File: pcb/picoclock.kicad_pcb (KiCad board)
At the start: 2 copper layers, 175.8 x 64 mm, 63 parts, among them J1 UART, J10 USB, J11 Alt Power, J12 PWM, J2 AUDIO, J3 xx, J4 xx, J5 Power In, J6 USB_C_Receptacle, J7 xx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

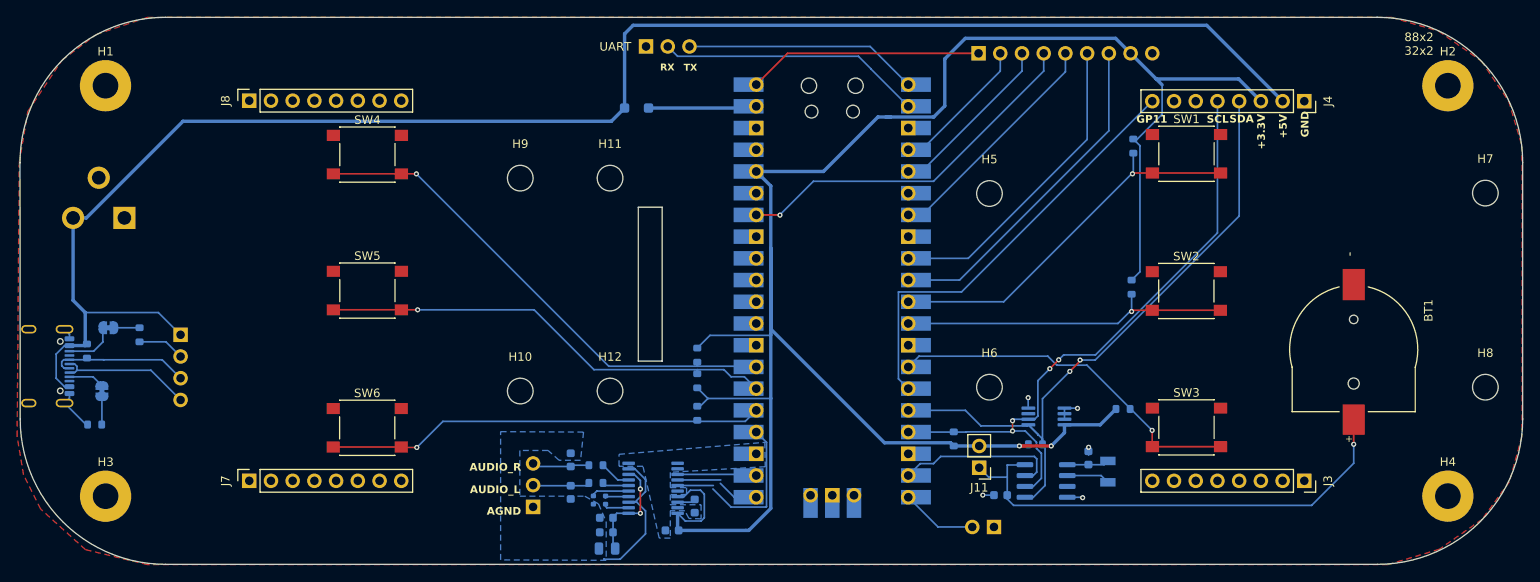
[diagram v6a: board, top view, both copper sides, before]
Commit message: [pcb] fix PCM5100 layout, AVDD, improvements
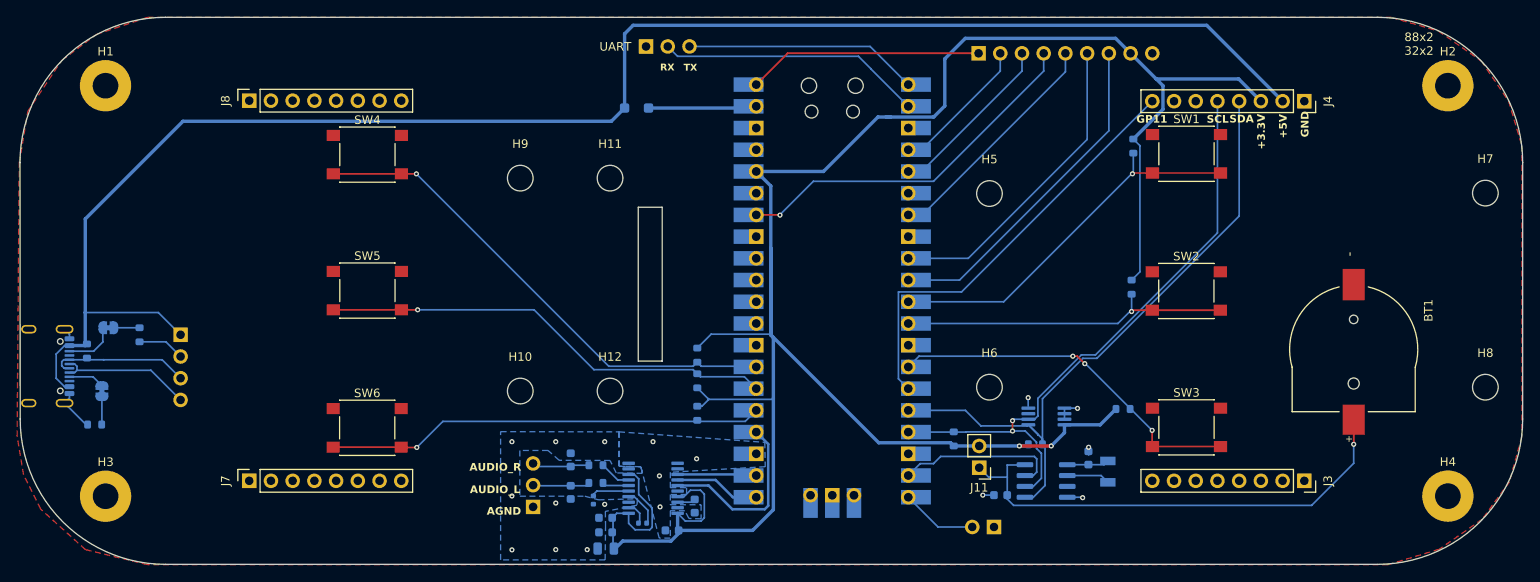
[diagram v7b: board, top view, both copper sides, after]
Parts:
- removed J5: Power In, Connector_BarrelJack:BarrelJack_CUI_PJ-102AH_Horizontal
- moved C7 5.10 mm to (131.7, 126.0), turned to 0 degrees
- moved C6 0.15 mm to (127.4, 129.0)
- moved C4 0.09 mm to (127.4, 127.1)
- moved C5 0.09 mm to (127.4, 125.4)
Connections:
- BT1 pad 2: GND -> AGND
- C1 pad 1: GND -> AGND
- C2 pad 2: GND -> AGND
- C3 pad 1: GND -> AGND
- C4 pad 2: AVDD -> +3.3V
- C5 pad 2: AVDD -> +3.3V
- C6 pad 1: AVDD -> +3.3V
- C9 pad 2: GND -> AGND
- H1 pad 1: GND -> AGND
- H2 pad 1: GND -> AGND
- H3 pad 1: GND -> AGND
- H4 pad 1: GND -> AGND
- J1 pad 1: GND -> AGND
- J10 pad 2: GND -> AGND
- J12 pad 1: GND -> AGND
- J3 pad 1: GND -> AGND
- J4 pad 1: GND -> AGND
- J6 pad A1: GND -> AGND
- J6 pad A12: GND -> AGND
- J6 pad B1: GND -> AGND
- J6 pad B12: GND -> AGND
- J6 pad S1: GND -> AGND
- J7 pad 1: GND -> AGND
- J8 pad 1: GND -> AGND
- J9 pad 9: GND -> AGND
- R5 pad 2: GND -> AGND
- R6 pad 2: GND -> AGND
- SW1 pad 1: GND -> AGND
- SW2 pad 1: GND -> AGND
- SW3 pad 1: GND -> AGND
- SW4 pad 1: GND -> AGND
- SW5 pad 1: GND -> AGND
- SW6 pad 1: GND -> AGND
- U1 pad 4: GND -> AGND
- U2 pad 13: GND -> AGND
- U2 pad 18: GND -> AGND
- U2 pad 23: GND -> AGND
- U2 pad 28: GND -> AGND
- U2 pad 3: GND -> AGND
- U2 pad 33: GND -> AGND
- U2 pad 38: GND -> AGND
- U2 pad 42: GND -> AGND
- U2 pad 8: GND -> AGND
- U3 pad 4: GND -> AGND
- U3 pad 5: GND -> AGND
- U3 pad 6: GND -> AGND
- U3 pad 7: GND -> AGND
- U4 pad 1: AVDD -> +3.3V
- U4 pad 10: GND -> AGND
- U4 pad 11: GND -> AGND
- U4 pad 12: GND -> AGND
- U4 pad 16: GND -> AGND
- U4 pad 19: GND -> AGND
- U4 pad 8: AVDD -> +3.3V
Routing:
- net +3.3V: track 241.5 -> 269.1 mm
- net GND: track 19.8 -> 0.00 mm, vias 5 -> 0
- net AVDD: track 12.7 -> 0.00 mm, vias 2 -> 0
- net AGND: track 16.8 -> 19.8 mm, vias 0 -> 18
- net +5V: track 195.9 -> 193.8 mm
- net Net-(U4-CAPM): track 2.80 -> 4.47 mm
- net SCL: track 74.5 -> 73.2 mm, vias 4 -> 2
- net LRCK: track 20.6 -> 21.1 mm
- net SDA: track 78.1 -> 77.9 mm, vias 2 -> 0
- net GPIO10: vias 1 -> 3
- added copper zone on F.Cu, net AGND
- removed copper zone on B.Cu, net GND
- removed copper zone on F.Cu, net GND

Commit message: [pcb] add sdcard: had to move PCM5100, other
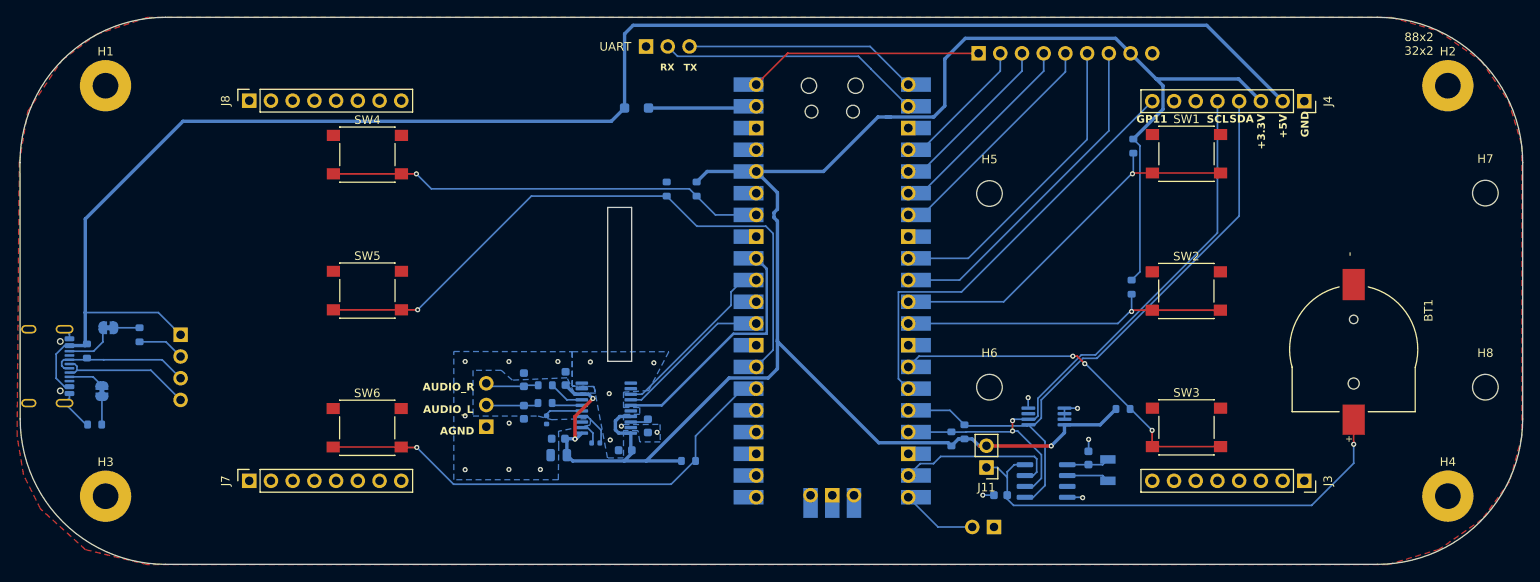
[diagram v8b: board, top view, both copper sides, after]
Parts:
- removed H10, H11, H12, H9: screen_adapter2, MountingHole:MountingHole_3mm
- moved R10 22.7 mm to (134.5, 87.0), turned to -90 degrees
- moved R9 19.4 mm to (138.0, 87.0)
- moved C5 17.0 mm to (122.7, 109.1), turned to -90 degrees
- moved C4 12.3 mm to (121.8, 116.2)
- moved C6 12.2 mm to (121.9, 118.1)
- moved R2 11.1 mm to (120.3, 112.0)
- moved R4 11.1 mm to (120.3, 109.9)
- moved C9 10.9 mm to (132.3, 114.7)
- moved C8 10.9 mm to (120.5, 114.0)
- moved J2 10.9 mm to (113.4, 114.8)
- moved C10 10.9 mm to (117.8, 113.1)
- moved C11 10.9 mm to (117.8, 109.3)
- moved C3 10.9 mm to (129.7, 117.5)
- moved C7 10.9 mm to (126.2, 116.7)
- moved U4 10.9 mm to (127.5, 112.6)
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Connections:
- net AGND renamed GND
- J9 pad 4: GPIO28 DC -> GPIO4 DC
- R10 pad 2: GPIO20 -> GPIO21/btn
- R11 pad 2: GPIO19 -> GPIO20/btn
- R9 pad 2: GPIO21 -> GPIO28/btn
- SW4 pad 2: GPIO21 -> GPIO28/btn
- SW5 pad 2: GPIO20 -> GPIO21/btn
- SW6 pad 2: GPIO19 -> GPIO20/btn
- U2 pad 21: DIN -> SD_D0_MISO
- U2 pad 22: BCK -> SD_D3_CS
- U2 pad 24: LRCK -> SD_CLK
- U2 pad 25: GPIO19 -> SD_CMD_MOSI
- U2 pad 26: GPIO20 -> GPIO20/btn
- U2 pad 27: GPIO21 -> GPIO21/btn
- U2 pad 29: unconnected-(U2-GPIO22-Pad29) -> DIN
- U2 pad 31: unconnected-(U2-GPIO26_ADC0-Pad31) -> BCK
- U2 pad 32: unconnected-(U2-GPIO27_ADC1-Pad32) -> LRCK
- U2 pad 34: GPIO28 DC -> GPIO28/btn
- U2 pad 6: unconnected-(U2-GPIO4-Pad6) -> GPIO4 DC
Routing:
- net GPIO21/btn: track 0.00 -> 75.4 mm, vias 0 -> 1
- net GPIO21: track 59.2 -> 0.00 mm, vias 1 -> 0
- net GPIO20/btn: track 0.00 -> 57.5 mm, vias 0 -> 1
- net GPIO20: track 53.4 -> 0.00 mm, vias 1 -> 0
- net GPIO28/btn: track 0.00 -> 51.4 mm, vias 0 -> 1
- net GPIO19: track 51.3 -> 0.00 mm, vias 1 -> 0
- net GPIO28 DC: track 42.8 -> 0.00 mm, vias 1 -> 0
- net +3.3V: track 269.1 -> 234.1 mm, vias 2 -> 3
- net GPIO4 DC: track 0.00 -> 23.8 mm
- net BCK: track 10.2 -> 21.1 mm
- net DIN: track 10.0 -> 18.4 mm
- net LRCK: track 21.1 -> 28.7 mm
- net SDA: track 77.9 -> 75.1 mm
- net 3V BATT: track 57.9 -> 56.6 mm
- net SD_D3_CS: track 0.00 -> 1.19 mm
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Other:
- outline, holes or cut-outs redrawn
